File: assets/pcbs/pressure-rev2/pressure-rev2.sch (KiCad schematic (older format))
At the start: 21 parts, among them J1 40HAT, J2 Conn_01x04, J3 Conn_02x01, J4 Conn_01x03, U1 TL7660, U2 INA126, U3 MINI-P-Sensor, U4 Adafruit_ADS1115, U5 MINI-P-Sensor, U6 MINI-P-Sensor

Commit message: revised, added schematic images
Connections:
- net at TP2.1, U5.3 (V_out): now also U4.8 (A1); no longer U4.7 (A0)
- net at TP1.1, U3.3 (V_out): now also U4.7 (A0); no longer U4.8 (A1)
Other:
- note added: "Airway\nPressure\nSensor"
- note added: "Auxiliary\nPressure\nSensor (unused)"
- note added: "Connector \nfor I2C"
- note added: "Differential\nPressure\nSensor (flow)"
- note added: "People's Ventilator Project\nSensor PCB v2\nAugust 19, 2020"
- note removed: "Connector \nfor Mass Flow Meter"
- note removed: "Connector \nfor additional analog input"
- note removed: "Jumper to select\nI2C address"
- note removed: "To use Oxygen sensor directly, \nuse ADC in differential \nmode with A2 and A3. \nConnect pin 3 to pin 6 \nwith jumper cable.\n"
- note removed: "To use Oxygen sensor directly, use ADC in differential mode with A2 and A3. \nConnect pin 2 of this header to pin 2 of INA with jumper cable.\n"
- moved on the sheet: C1, C2, J2, J3, J4, R1, U1, U2

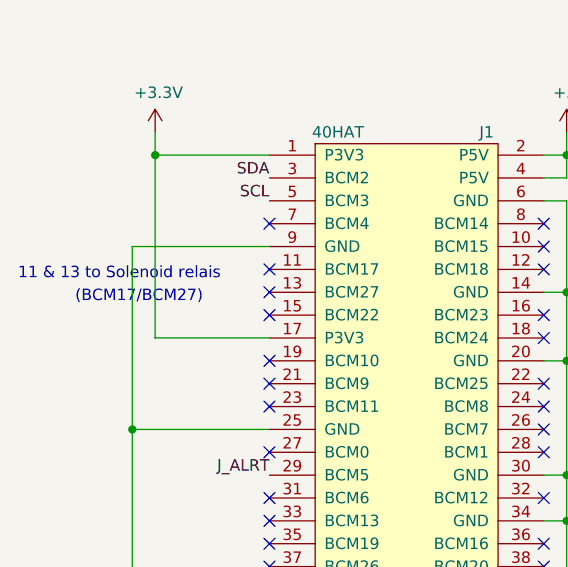
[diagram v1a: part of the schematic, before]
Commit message: update schematic img and file for sensor board
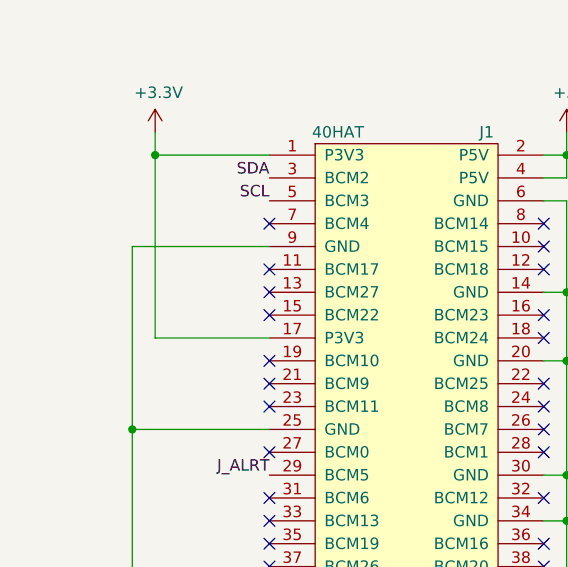
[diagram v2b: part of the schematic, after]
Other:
- note removed: "(BCM17/BCM27)\n"
- note removed: "11 & 13 to Solenoid relais"
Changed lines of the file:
@@
 Text Label 2050 3700 2    50   ~ 0
 J_ALRT
-Text Notes 1200 2950 0    50   ~ 0
-(BCM17/BCM27)\n
 NoConn ~ 2050 2600
 NoConn ~ 2050 3000
@@
 	1    0    0    -1
 $EndComp
-Text Notes 950  2850 0    50   ~ 0
-11 & 13 to Solenoid relais
 NoConn ~ 2050 2900
 NoConn ~ 2050 2800
